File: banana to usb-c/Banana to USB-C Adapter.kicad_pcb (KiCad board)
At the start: 2 copper layers, 34.3 x 26.6 mm, 32 parts, among them J1 Barrel_Jack_Switch, J2 Positive, J3 Negative

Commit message: pcb updated with usb-c components, 7 unrouted. yikes.
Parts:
- removed the REF** at (151.2, 106.4)
- removed the REF** at (151.2, 106.2)
- added R3: 5k1, Resistor_SMD:R_1206_3216Metric_Pad1.30x1.75mm_HandSolder, B.Cu at (150.0, 102.3)
- added R4: 5k1, Resistor_SMD:R_1206_3216Metric_Pad1.30x1.75mm_HandSolder, B.Cu at (150.0, 96.9)
- J1: value Barrel_Jack_Switch -> USB4125-GF-A-0190; footprint Connector_BarrelJack:BarrelJack_GCT_DCJ200-10-A_Horizontal -> Connector_USB:USB_C_Receptacle_GCT_USB4125-xx-x_6P_TopMnt_Horizontal
- moved J1 4.56 mm to (156.2, 99.2)
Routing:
- net Net-(J1-CC1): track 0.00 -> 4.71 mm, vias 0 -> 1
- net Net-(J1-CC2): track 0.00 -> 4.46 mm, vias 0 -> 1

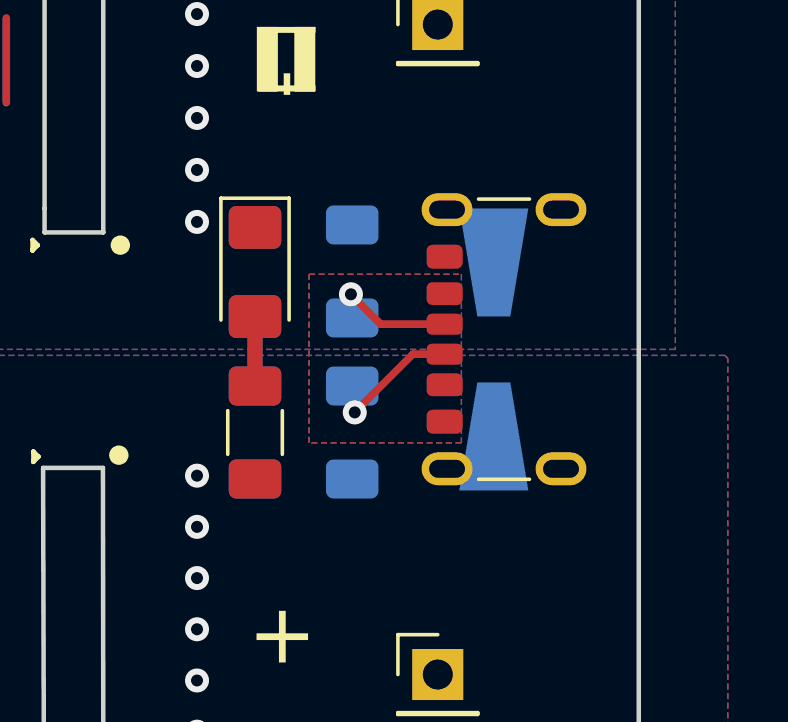
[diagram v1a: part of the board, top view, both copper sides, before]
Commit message: usb-c ready for fab
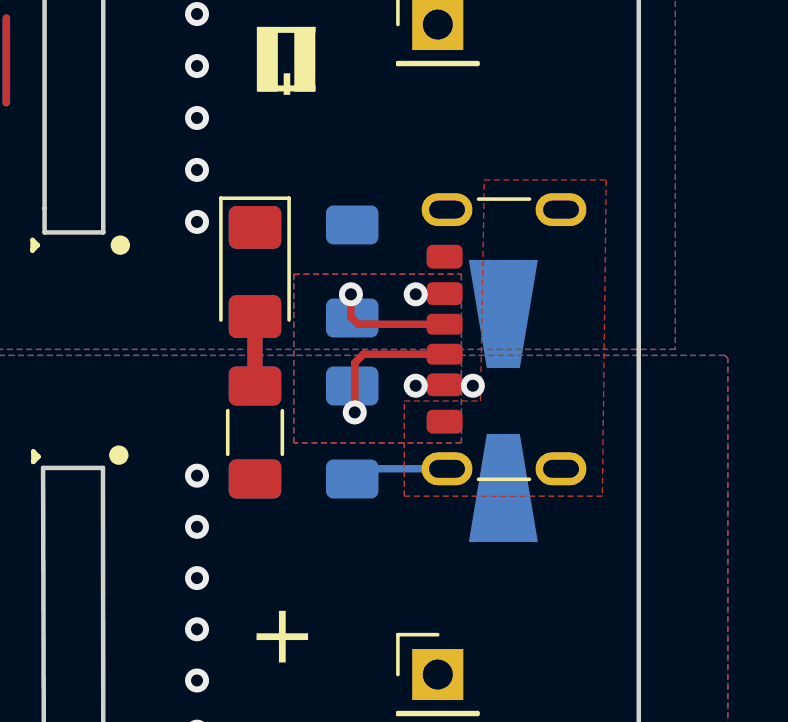
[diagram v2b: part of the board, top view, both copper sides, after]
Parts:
- moved D3 1.75 mm to (155.1, 101.2)
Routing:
- net GND: track 5.60 -> 8.90 mm
- net /Positive: track 0.00 -> 2.90 mm, vias 6 -> 9
- net Net-(J1-CC1): track 4.71 -> 5.68 mm
